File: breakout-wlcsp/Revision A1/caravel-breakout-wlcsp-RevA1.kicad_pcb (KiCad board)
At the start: 2 copper layers, 45 x 52.5 mm, 42 parts, among them CON1 REF-182665-01, CON2 REF-182665-01, CON3 73251-1352, U1 Caravel, U2 TLV73318PDBV

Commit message: initial check-in for RevA1
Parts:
- removed C8, C9: 0.1uf, Capacitor_SMD:C_0603_1608Metric
- removed U2: TLV73318PDBV, Package_TO_SOT_SMD:SOT-23-5
- moved C7 1.53 mm to (27.4, -30.9)
- moved C1 1.17 mm to (19.5, -31.8)
- moved C5 0.81 mm to (22.0, -22.9)
- moved C6 0.41 mm to (27.4, -29.8), turned to 180 degrees
- moved C2 0.40 mm to (22.6, -32.6)
- moved C4 0.29 mm to (24.8, -23.2)
- moved C3 0.07 mm to (19.1, -24.6), turned to 180 degrees
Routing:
- net vddio: track 2.14 -> 43.2 mm, vias 0 -> 3
- net mprj_io[8]: track 1.43 -> 38.5 mm, vias 0 -> 2
- net ~{RST}: track 0.75 -> 37.0 mm, vias 1 -> 2
- net mprj_io[10]: track 1.32 -> 35.6 mm
- net xclk: track 1.46 -> 33.1 mm
- net mprj_io[12]: track 1.24 -> 32.7 mm
- net mprj_io[36]: track 3.09 -> 33.0 mm
- net vccd2: track 1.77 -> 31.4 mm, vias 0 -> 3
- net mprj_io[32]: track 1.27 -> 30.9 mm
- net mprj_io[9]: track 1.96 -> 31.1 mm
- net mprj_io[34]: track 3.04 -> 31.6 mm
- net mprj_io[11]: track 1.88 -> 28.3 mm
- net mprj_io[37]: track 2.46 -> 26.5 mm
- net mprj_io[14]: track 2.96 -> 26.7 mm
- net vccd: track 2.59 -> 26.3 mm, vias 1 -> 3
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- added copper zone on B.Cu, net GND
- added copper zone on F.Cu, net GND
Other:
- outline, holes or cut-outs redrawn
- board text added: "[this side down] be careful which way around this gets plugged in!"
- board text added: "caravel-breakout-wlcsp RevA1"
- board text added: "ok'23"
- board text added: "tinytapeout.com"
- board text added: "zerotoasic course.com"
- board text removed: "(this side down)"
- board text removed: "ok'22"

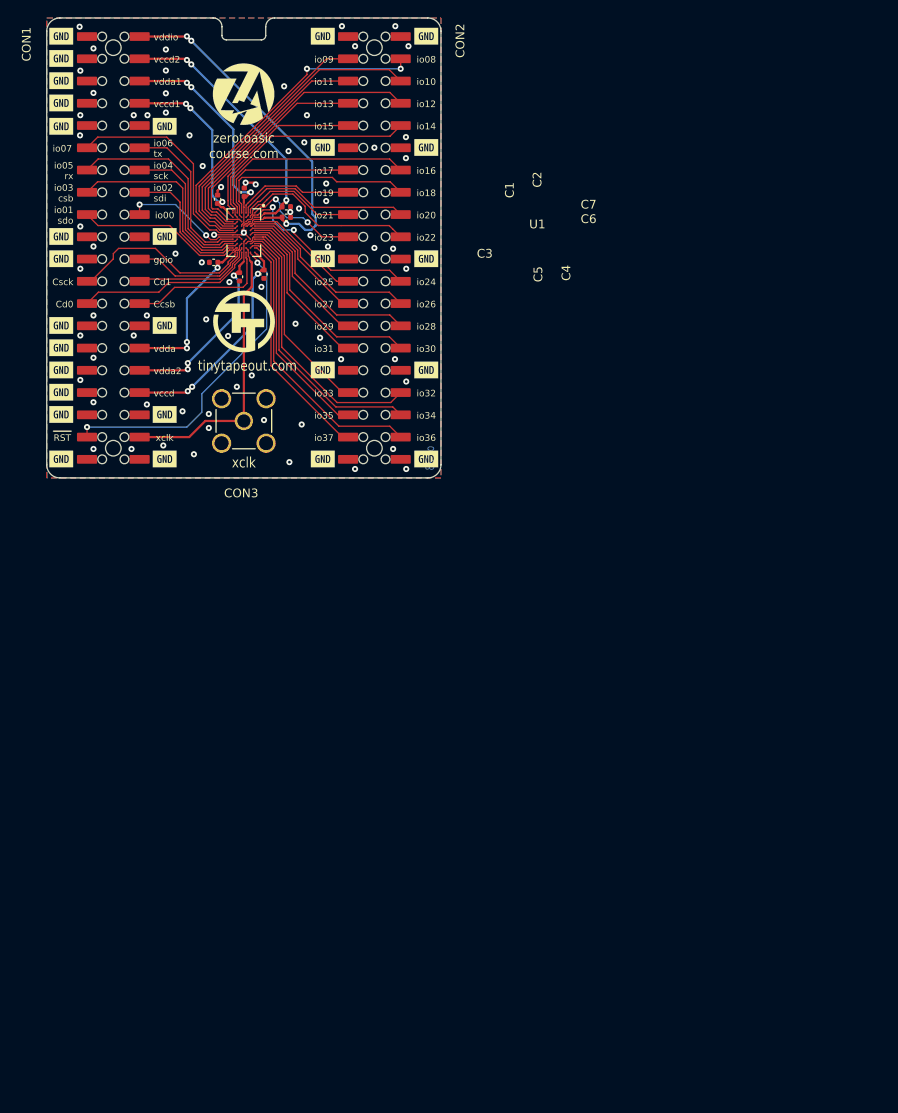
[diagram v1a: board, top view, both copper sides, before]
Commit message: Update to logos, resource refactor, kicad 7 migration
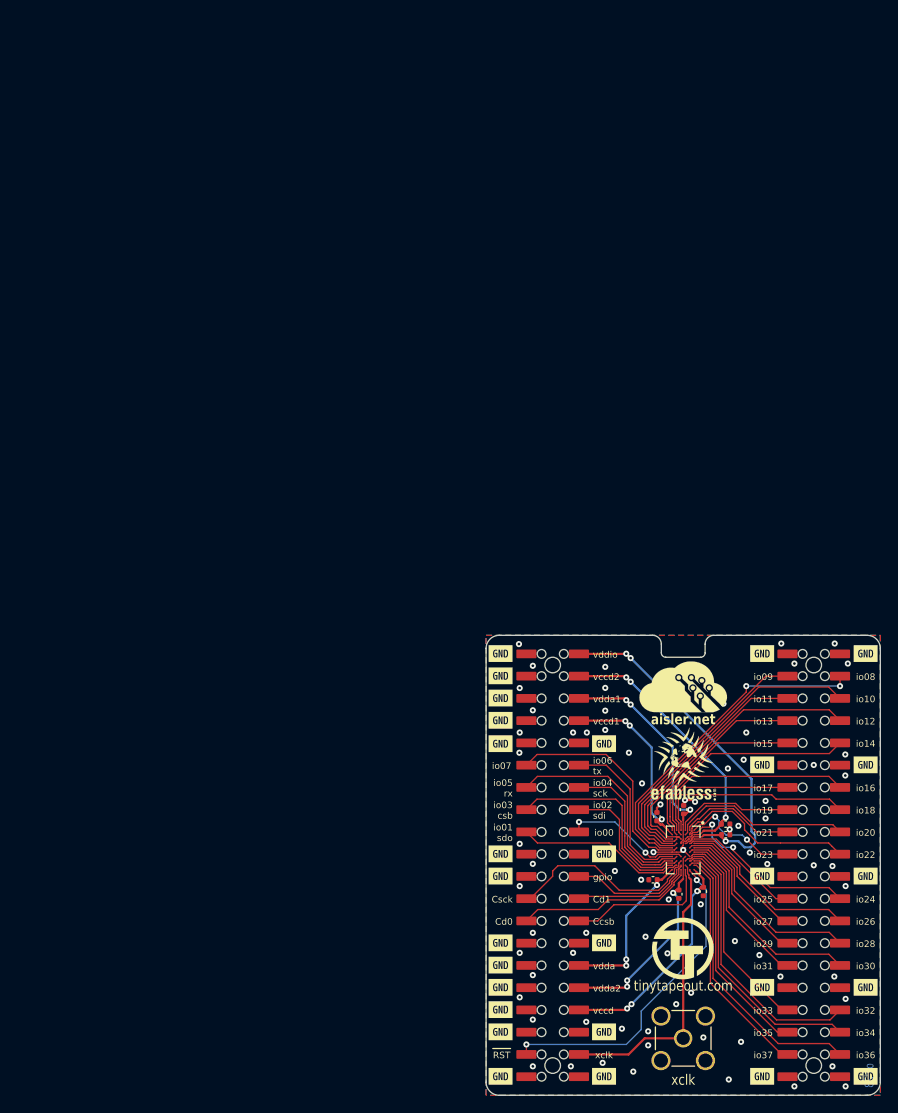
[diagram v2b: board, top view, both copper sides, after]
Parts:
- added REF**: Logo, Logos:ef_logo_graphical, F.Cu at (72.7, 31.9)
- added REF**: Logo, Logos:ef_logo, F.Cu at (72.7, 36.0)
- added REF**: aisler_logo_10, Logos:aisler_logo_10, F.Cu at (72.9, 26.7)
- added REF**: TT_logo, Logos:TT_logo, F.Cu at (72.7, 53.8)
- moved kibuzzard-6288F08E 86.5 mm to (63.6, 68.3)
- moved kibuzzard-6288F08E 86.5 mm to (81.7, 68.3)
- moved C1 86.5 mm to (69.7, 38.7)
- moved C2 86.5 mm to (72.7, 37.9)
- moved C3 86.5 mm to (69.2, 45.9)
- moved C4 86.5 mm to (75.0, 47.2)
- moved C5 86.5 mm to (72.2, 47.5)
- moved C6 86.5 mm to (77.5, 40.7)
- moved C7 86.5 mm to (77.5, 39.5)
- moved CON1 86.5 mm to (57.8, 44.2)
- moved CON2 86.5 mm to (87.5, 44.2)
- moved CON3 86.5 mm to (72.7, 64.0)
- moved U1 86.5 mm to (72.7, 42.5)
- moved kibuzzard-6288F08E 86.5 mm to (63.6, 63.2)
- moved kibuzzard-6288F08E 86.5 mm to (51.8, 53.1)
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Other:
- board text added: "aisler.net"
- board text added: "caravel-breakout-wlcsp RevA2"
- board text removed: "caravel-breakout-wlcsp RevA1"
- board text removed: "zerotoasic course.com"
